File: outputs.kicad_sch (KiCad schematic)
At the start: 22 parts, among them J2 Conn_01x06, Q1 SSM3K357R, Q2 SSM3K357R, Q3 SSM3K357R, U7 VNLD5090, U9 VNLD5090

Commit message: Populate Board
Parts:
- removed D16, D19: D, Diode_SMD:D_SOD-123F, symbol Device:D
- removed J2: Conn_01x06, Connector_PinHeader_2.54mm:PinHeader_1x06_P2.54mm_Vertical, symbol Connector_Generic:Conn_01x06
- removed R53, R56, R57: 1k, Resistor_SMD:R_0805_2012Metric, symbol Device:R
- removed R60, R61: 100k, Resistor_SMD:R_0805_2012Metric, symbol Device:R
- removed U7, U9: VNLD5090, Package_SO:SO-8_3.9x4.9mm_P1.27mm, symbol IC_Automotive:VNLD5090
- added D6, D7: D, Diode_SMD:D_SOD-123F, symbol Device:D
- added J3: Conn_01x04, Connector_PinHeader_2.54mm:PinHeader_1x04_P2.54mm_Vertical, symbol Connector_Generic:Conn_01x04
- added J4: Conn_01x02, Connector_PinHeader_2.54mm:PinHeader_1x02_P2.54mm_Vertical, symbol Connector_Generic:Conn_01x02
- added R49, R51: 100k, Resistor_SMD:R_0805_2012Metric, symbol Device:R
- added R50: 1k, Resistor_SMD:R_0805_2012Metric, symbol Device:R
- added R54: 4k7, Resistor_SMD:R_0805_2012Metric, symbol Device:R
- added U10, U7, U8, U9: VNL5050, IC_Automotive:SOT-223-3_VNL5050, symbol IC_Automotive:VNL5050N3TR
- added U11: MCP2551-I-SN, Package_SO:SOIC-8_3.9x4.9mm_P1.27mm, symbol Interface_CAN_LIN:MCP2551-I-SN
- R52: value 2k -> 1k; Digikey Part Number 311-2.00KCRCT-ND -> 311-1.00KCRCT-ND; Manufacturer_Part_Number RC0805FR-072KL -> RC0805FR-071KL; URL https://www.digikey.com/product-detail/en/yageo/RC0805FR-072KL/311-2.00KCRCT-ND/730611 -> https://www.digikey.com/product-detail/en/yageo/RC0805FR-071KL/311-1.00KCRCT-ND/730391
- renumbered D17 to D4, D18 to D5, Q2 to Q1, Q3 to Q2, Q1 to Q3, R49 to R45, R47 to R46, R50 to R47, R51 to R53
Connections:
- net BOOST-OUT: now also U7.2 (D)
- net GND: now also R47.2, J3.3 (Pin_3), R49.2, R51.2, R54.1, U10.3 (S), U11.2 (VSS), U7.3 (S), U8.3 (S), U9.3 (S); no longer R47.1, R52.2
- net HC-1-OUT: now also D6.2 (A), U9.2 (D); no longer D5.2 (A)
- net HC-2-OUT: now also D7.2 (A), U10.2 (D)
- net IDLE-OUT: now also D5.2 (A), U8.2 (D)
- net at R46.1: now also U7.1 (IN)
- net at R48.1: now also U8.1 (IN)
- net at R52.1: now also U10.1 (IN)
- net 12V-SW renamed +12V
- net +12V: now also D6.1 (K), D7.1 (K)
- net FAN-OUT renamed FAN-OUT-D
- net FUELPUMP-OUT renamed FUELPUMP-OUT-D
- net MCU-D16 renamed MCU-STEPPER-DIR-D
- net MCU-D17 renamed MCU-STEPPER-STEP-D
- net MCU-D24 renamed MCU-STEPPER-EN-D
- net MCU-D45 renamed FUELPUMP-TRIG
- net MCU-D47 renamed FAN-TRIG
- net MCU-D49 renamed TACHO-TRIG
- net MCU-D6 renamed IDLE-TRIG
- net IDLE-TRIG: now also R47.1; no longer R47.2
- net MCU-D7 renamed BOOST-TRIG
- net TACHO-OUT renamed TACHO-OUT-D
- net VDD renamed +5V
- net +5V: now also J3.4 (Pin_4), U11.3 (VDD)
- new net: R54.2, U11.8 (Rs)
- new net: R50.1, U9.1 (IN)
- new net EXT-CAN-H: J4.1 (Pin_1), U11.7 (CANH)
- new net EXT-CAN-L: J4.2 (Pin_2), U11.6 (CANL)
- new net HC1-TRIG: R49.1, R50.2
- new net HC2-TRIG: R51.1, R52.2
- new net MCU-CAN-RX: U11.4 (RXD)
- new net MCU-CAN-TX: U11.1 (TXD)
- new net MCU-UART-RX-BT: J3.2 (Pin_2)
- new net MCU-UART-TX-BT: J3.1 (Pin_1)
- no-connect marks 0 -> 5
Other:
- note added: "12V use?"
- note added: "Boost Output"
- note added: "Can Converter / Protection"
- note added: "Fan Output"
- note added: "Filter 5V?"
- note added: "Fuel Pump Output"
- note added: "PWM Idle Output"
- note added: "Spare High Current Outputs"
- note added: "TODO: Check"
- note added: "Tacho Output"
- note removed: "Fan and Fuel Pump outputs"
- note removed: "PWM Idle and Boost outputs"
- note removed: "Spare High Current outputs"
- note removed: "Tacho output"
- moved on the sheet: A1, D4, D5, Q1, Q2, Q3, R45, R46, R47, R48, R53

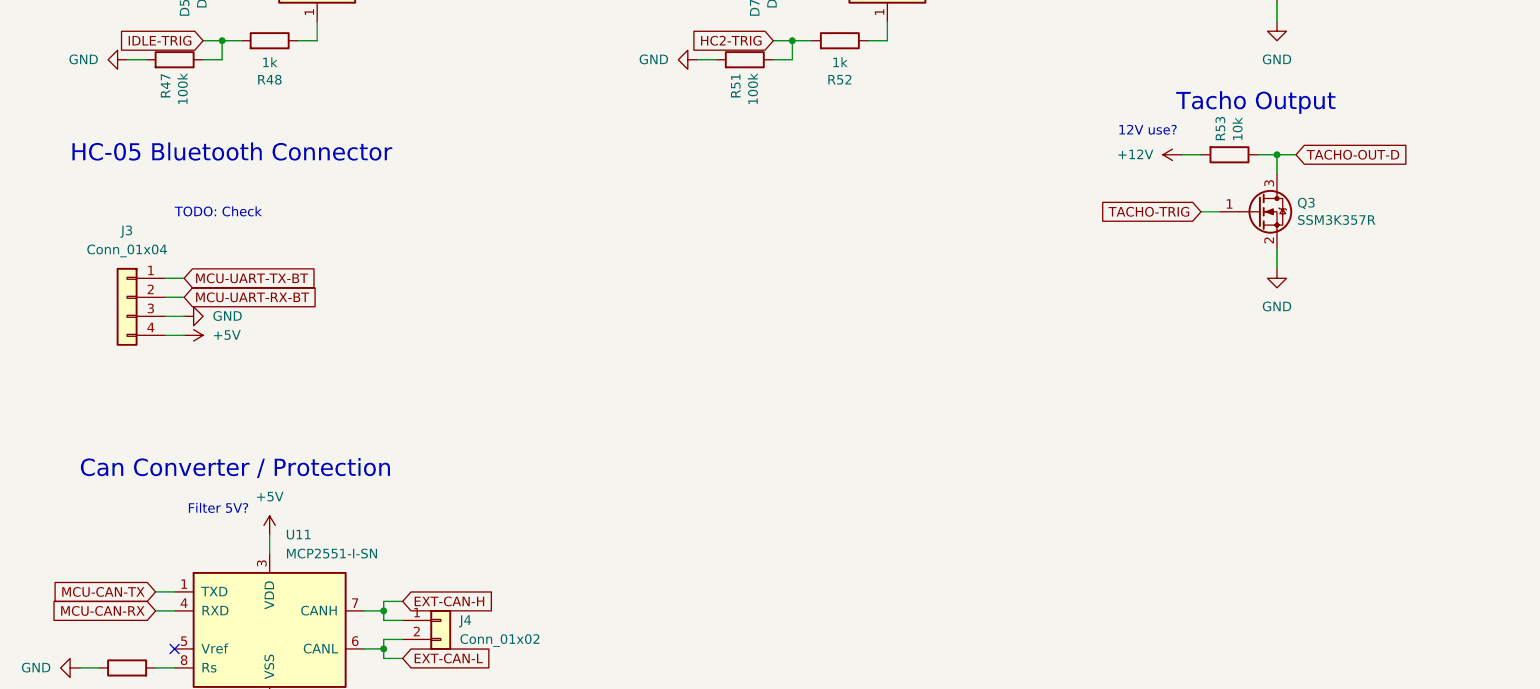
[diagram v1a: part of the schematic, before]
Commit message: Add additional IOs
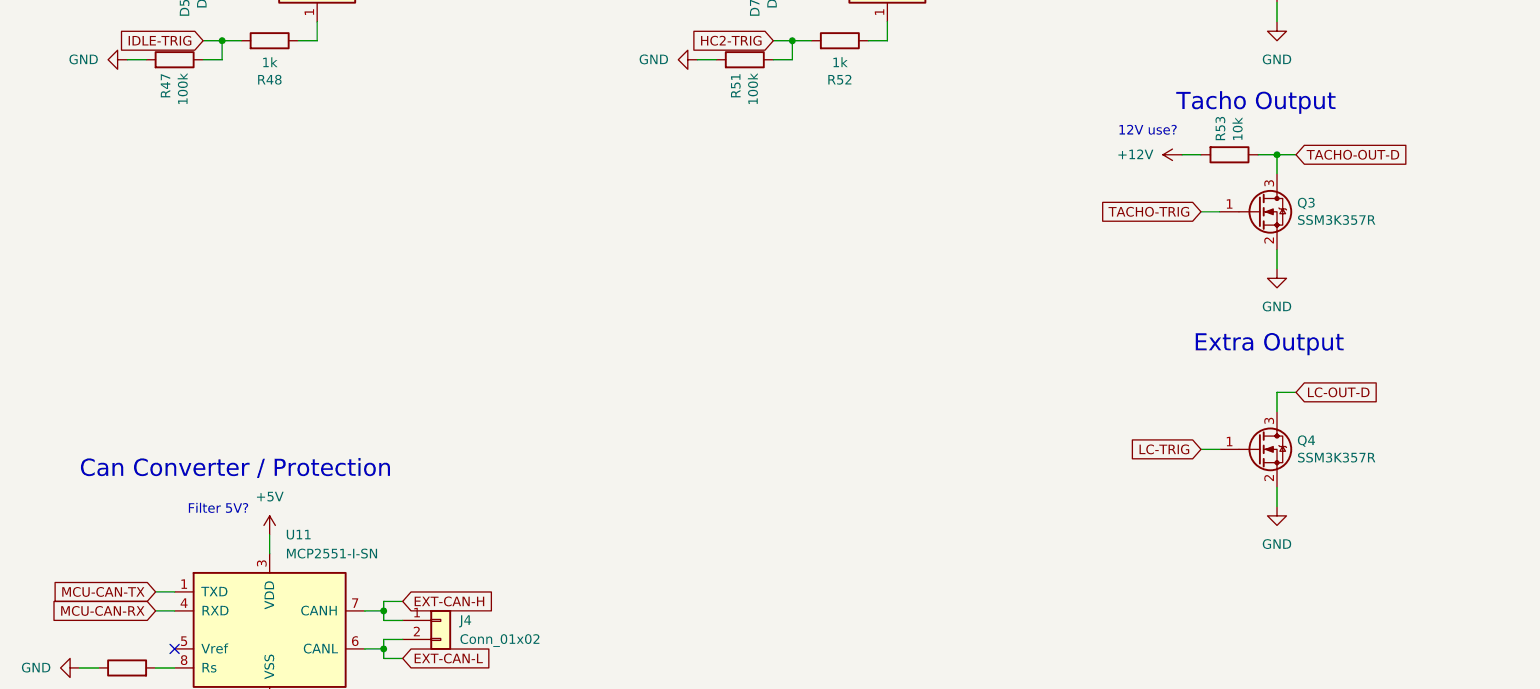
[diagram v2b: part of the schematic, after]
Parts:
- removed J3: Conn_01x04, Connector_PinHeader_2.54mm:PinHeader_1x04_P2.54mm_Vertical, symbol Connector_Generic:Conn_01x04
- added Q4: SSM3K357R, Package_TO_SOT_SMD:SOT-23, symbol Transistor_FET:2N7002
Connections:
- net GND: now also Q4.2 (S)
- new net LC-OUT-D: Q4.3 (D)
- new net LC-TRIG: Q4.1 (G)
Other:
- note added: "Extra Output"
- note removed: "HC-05 Bluetooth Connector"
- note removed: "TODO: Check"

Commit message: Pre MCU switch
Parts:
- removed U10, U7, U8, U9: VNL5050, IC_Automotive:SOT-223-3_VNL5050, symbol IC_Automotive:VNL5050N3TR
- added D22, D24, D26, D28: D, Diode_SMD:D_SOD-323, symbol Device:D
- added D23, D25, D27, D29: LED, LED_SMD:LED_0805_2012Metric, symbol Device:LED
- added IC3, IC4, IC5, IC6: VNL5090N3-E, SOT230P700X180-4N, symbol IC_Automotive:VNL5090N3-E
- added R94, R95, R96, R97: 2.4k, Resistor_SMD:R_0805_2012Metric, symbol Device:R
- D4, D5, D6, D7: footprint Diode_SMD:D_SOD-123F -> Diode_SMD:D_SOD-323; Digikey Part Number S110FACT-ND -> (none); Manufacturer_Name ONSEMI -> (none); Manufacturer_Part_Number S110FA -> (none); URL https://www.digikey.com/en/products/detail/on-semiconductor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 -> (none)
- R47, R49, R51: value 100k -> 1k; Digikey Part Number 311-100KCRCT-ND -> 311-1.00KCRCT-ND; Manufacturer_Part_Number RC0805FR-07100KL -> RC0805FR-071KL; URL https://www.digikey.com/product-detail/en/yageo/RC0805FR-07100KL/311-100KCRCT-ND/730491 -> https://www.digikey.com/product-detail/en/yageo/RC0805FR-071KL/311-1.00KCRCT-ND/730391
- R48, R50, R52: value 1k -> 100k; Digikey Part Number 311-1.00KCRCT-ND -> 311-100KCRCT-ND; Manufacturer_Part_Number RC0805FR-071KL -> RC0805FR-07100KL; URL https://www.digikey.com/product-detail/en/yageo/RC0805FR-071KL/311-1.00KCRCT-ND/730391 -> https://www.digikey.com/product-detail/en/yageo/RC0805FR-07100KL/311-100KCRCT-ND/730491
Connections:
- net +12V: now also R94.2, R95.2, R96.2, R97.2
- net BOOST-OUT: now also D22.1 (K), IC3.2 (DRAIN_1), IC3.4 (DRAIN_2)
- net GND: now also R48.2, R50.2, R52.2, IC3.3 (SOURCE), IC4.3 (SOURCE), IC5.3 (SOURCE), IC6.3 (SOURCE); no longer R47.2, R49.2, R51.2
- net HC-1-OUT: now also D26.1 (K), IC5.2 (DRAIN_1), IC5.4 (DRAIN_2)
- net HC-2-OUT: now also D28.1 (K), IC6.2 (DRAIN_1), IC6.4 (DRAIN_2)
- net HC1-TRIG: now also R49.2, R50.1; no longer R49.1, R50.2
- net HC2-TRIG: now also R51.2, R52.1; no longer R51.1, R52.2
- net IDLE-OUT: now also D24.1 (K), IC4.2 (DRAIN_1), IC4.4 (DRAIN_2)
- net IDLE-TRIG: now also R47.2, R48.1; no longer R47.1, R48.2
- net at R46.1: now also IC3.1 (INPUT)
- new net: D24.2 (A), D25.1 (K)
- new net: D26.2 (A), D27.1 (K)
- new net: D27.2 (A), R96.1
- new net: D25.2 (A), R95.1
- new net: D23.2 (A), R94.1
- new net: IC4.1 (INPUT), R47.1
- new net: D29.2 (A), R97.1
- new net: D28.2 (A), D29.1 (K)
- new net: D22.2 (A), D23.1 (K)
- new net: IC6.1 (INPUT), R51.1
- new net: IC5.1 (INPUT), R49.1
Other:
- moved on the sheet: J4, R45, R46, R54, U11

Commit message: Fully connect all components
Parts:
- added C53: 100nF, Capacitor_SMD:C_0805_2012Metric, symbol Device:C
- added C8: 22µF, Capacitor_SMD:C_0805_2012Metric, symbol Device:C
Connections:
- net +5V: now also C53.2
- net GND: now also C53.1, C8.1
- net +12V renamed VBAT
- net VBAT: now also C8.2
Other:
- note removed: "12V use?"
- note removed: "Filter 5V?"
- moved on the sheet: J4, Q1, Q2, Q3, Q4, R53, R54, U11

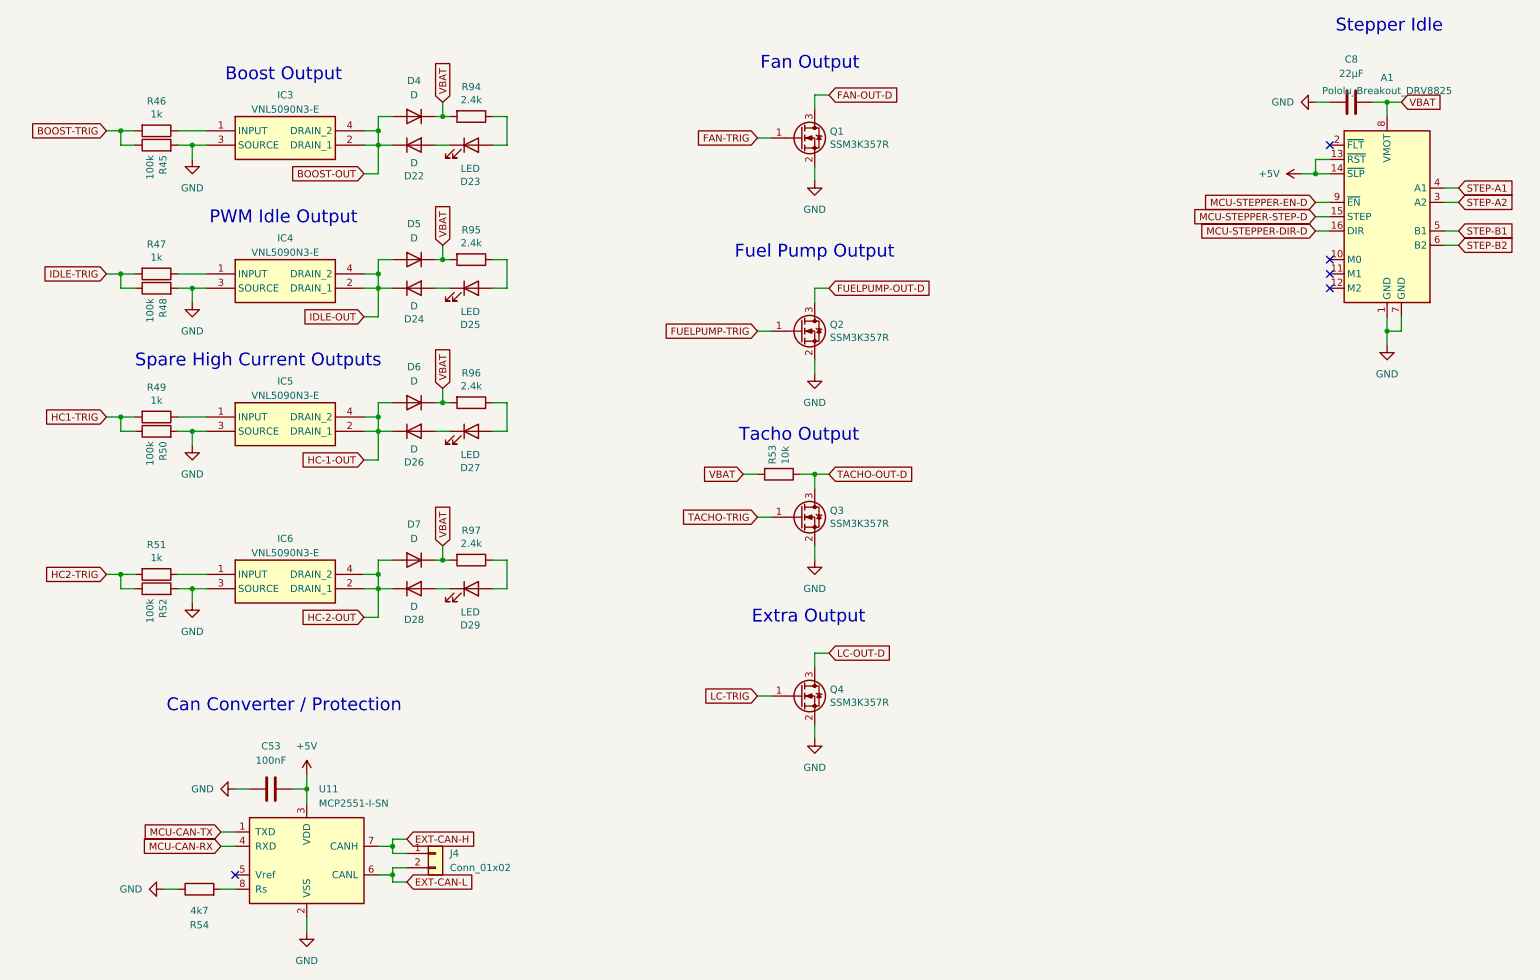
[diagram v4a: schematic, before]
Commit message: Updated reference layout
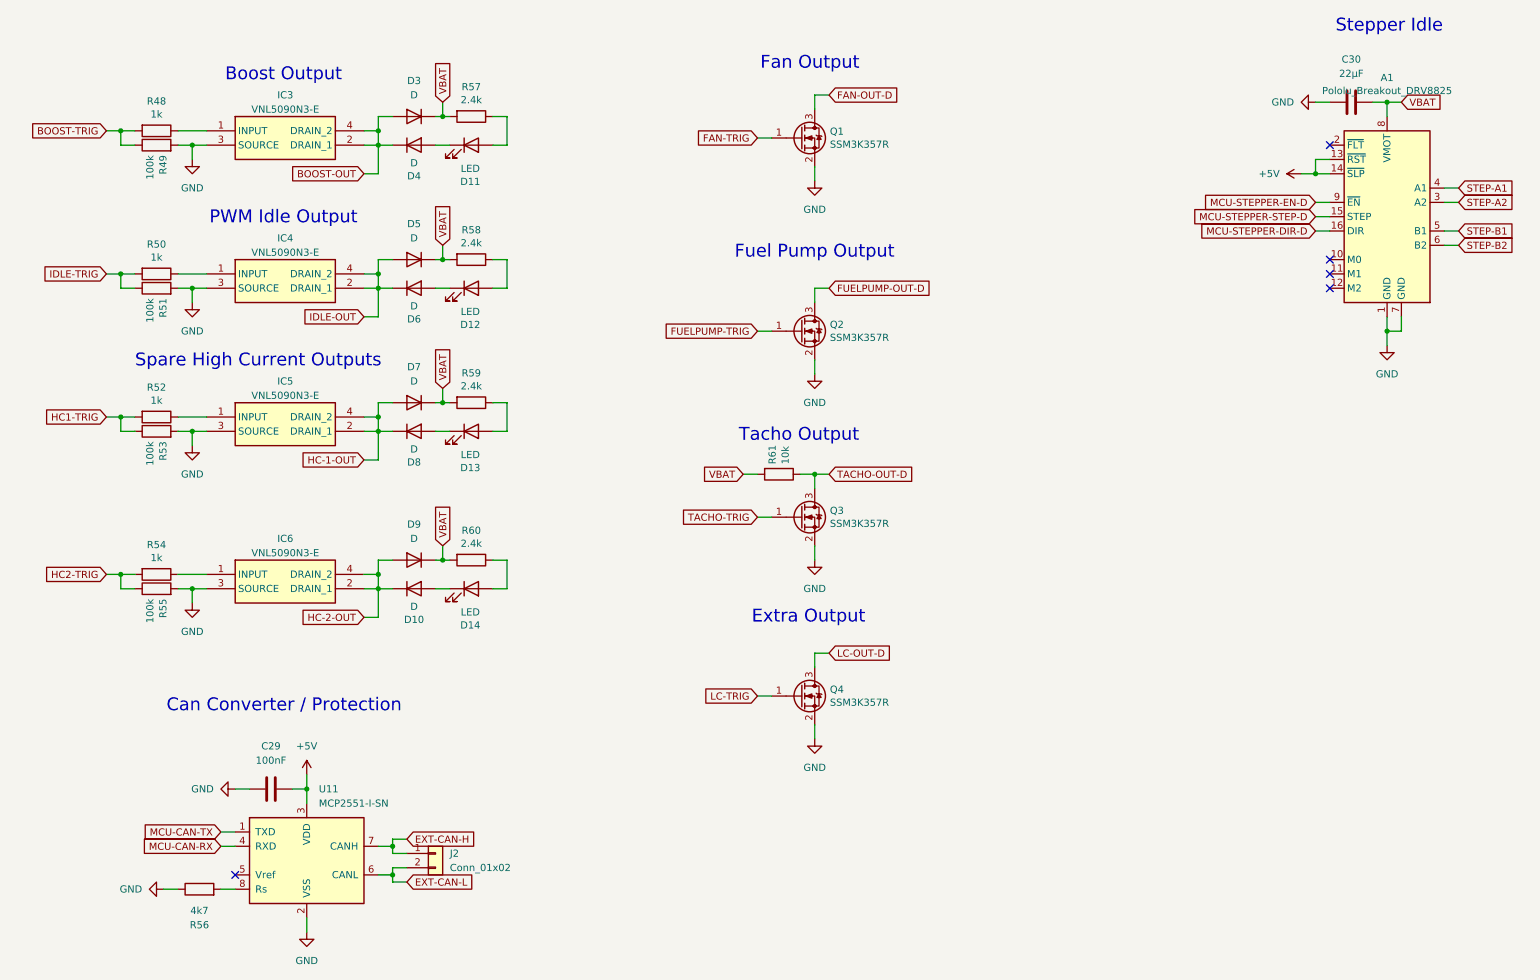
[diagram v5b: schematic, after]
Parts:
- renumbered C53 to C29, C8 to C30, D28 to D10, D23 to D11, D25 to D12, D27 to D13, D29 to D14, D4 to D3, D22 to D4, D24 to D6, D6 to D7, D26 to D8, D7 to D9, J4 to J2, R46 to R48, R45 to R49, R47 to R50, R48 to R51, R49 to R52, R50 to R53, R51 to R54, R52 to R55, R54 to R56, R94 to R57, R95 to R58, R96 to R59, R97 to R60, R53 to R61

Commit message: Change power layout, add low frequency crystal
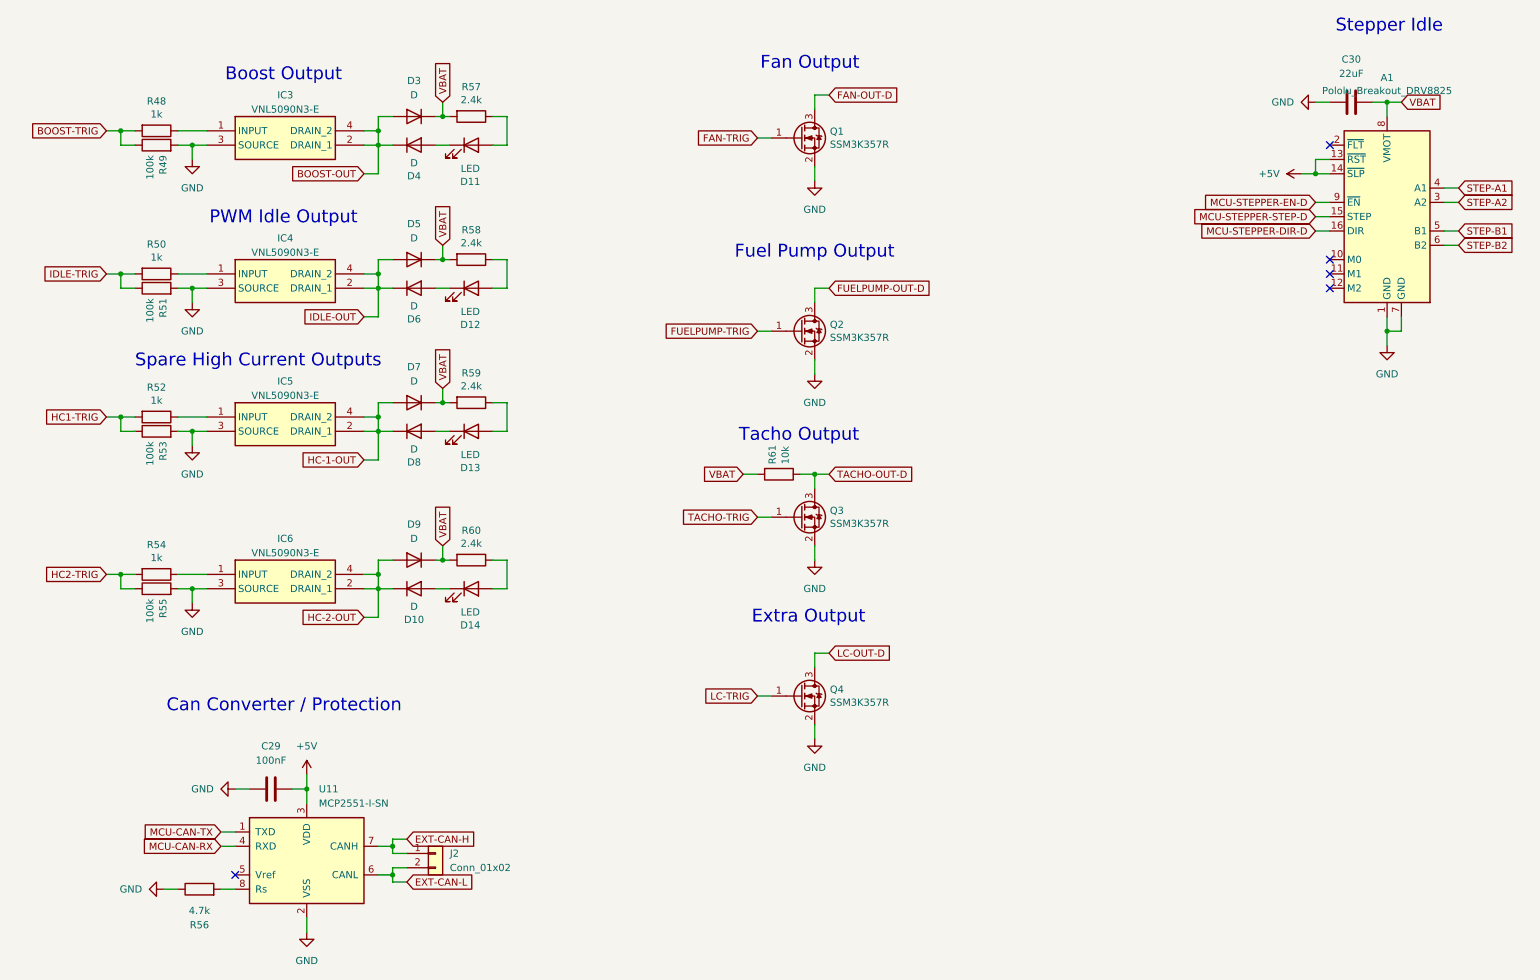
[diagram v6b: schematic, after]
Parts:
- C30: value 22µF -> 22uF
- R56: value 4k7 -> 4.7k
